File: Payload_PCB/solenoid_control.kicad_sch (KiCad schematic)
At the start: 9 parts, among them Q2 NMOS, Q29 NMOS

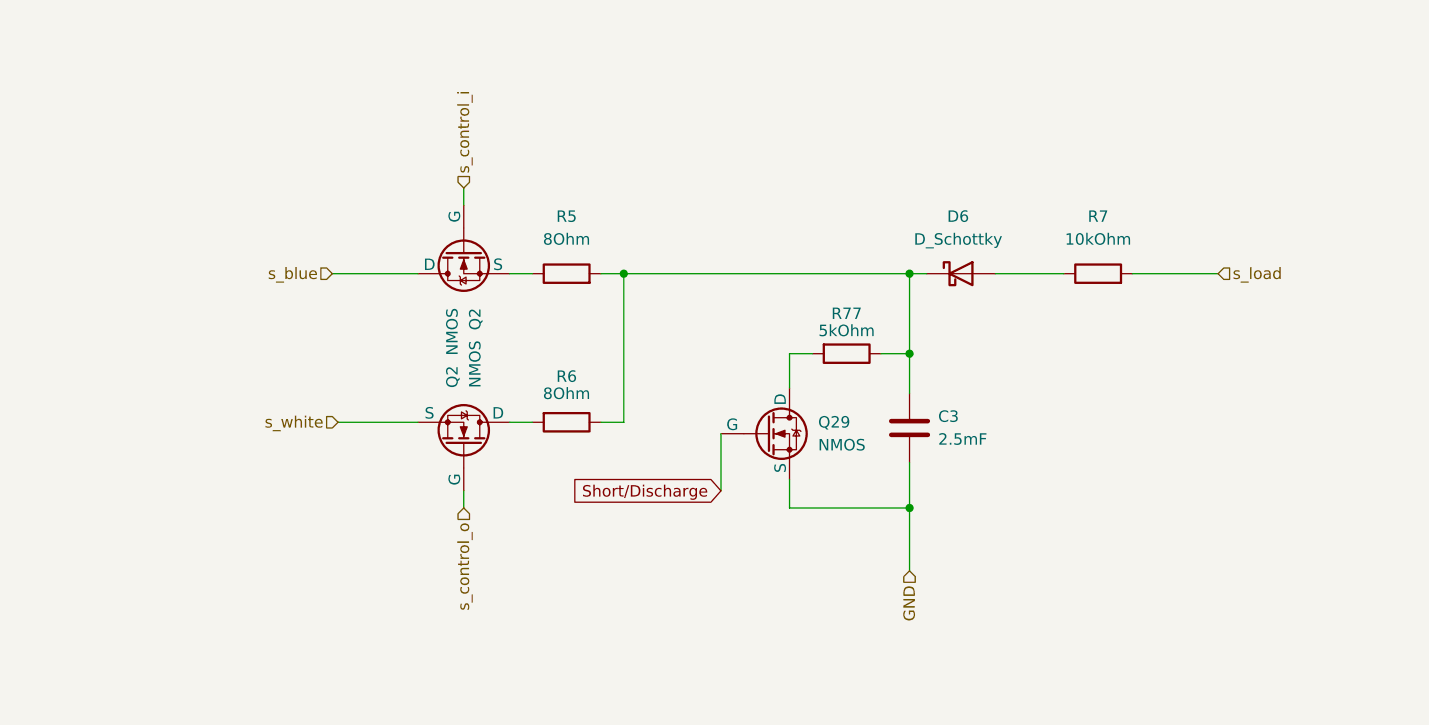
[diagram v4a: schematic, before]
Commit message: Added heating pad, adjustment of page sizes
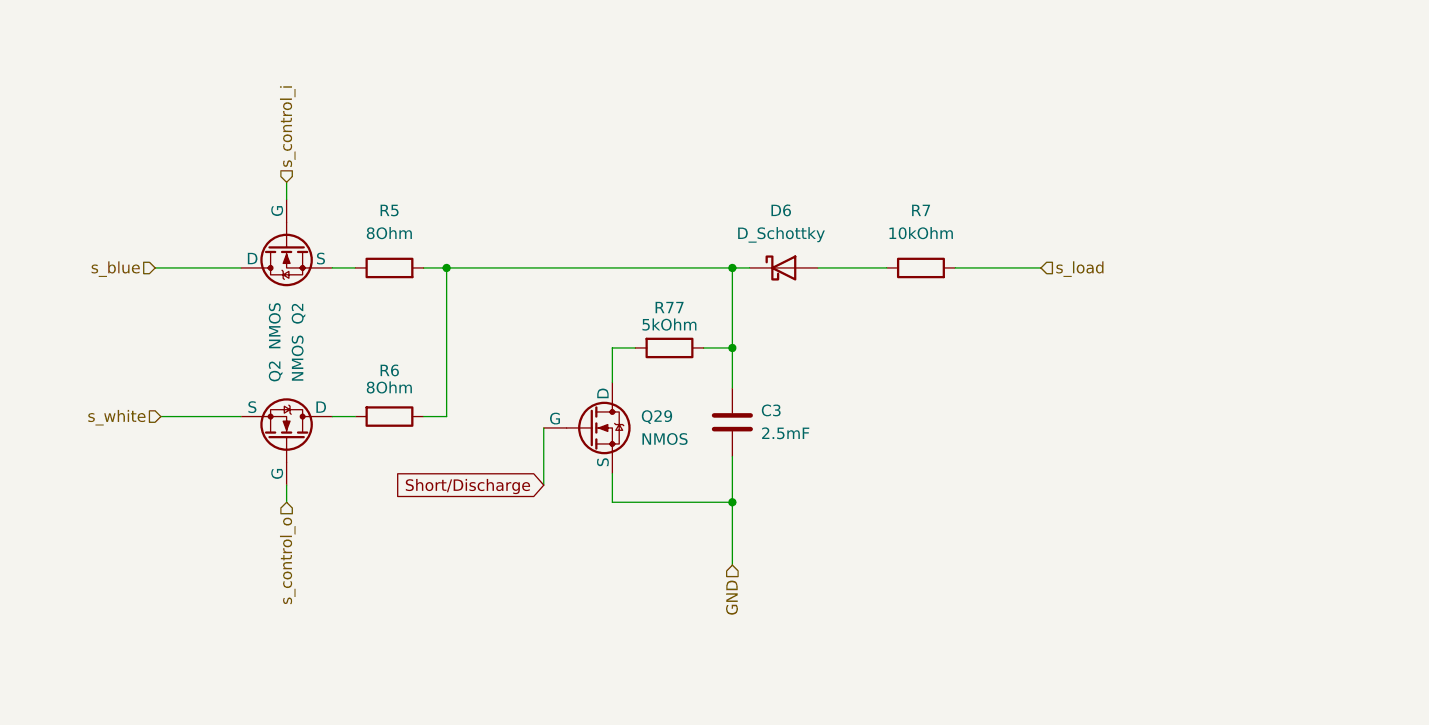
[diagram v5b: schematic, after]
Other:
- moved on the sheet: C3, D6, Q2, Q29, R5, R6, R7, R77

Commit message: Added some actual parts
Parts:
- removed D6: D_Schottky, symbol Device:D_Schottky
- removed Q2 (x2), Q29: NMOS, symbol Simulation_SPICE:NMOS
- added D6: RB511VM-30TE-17, RB511VM30TE17, symbol RB511VM-30TE-17:RB511VM-30TE-17
- added Q28, Q6: SI1308EDL-T1-BE3, SOT65P210X110-3N, symbol SI1308EDL-T1-BE3:SI1308EDL-T1-BE3
- added Q30: SSM3K36TU,LF, SOTFL65P210X75-3N, symbol SSM3K36TU_LF:SSM3K36TU,LF
- R77: value 5kOhm -> 10kOhm
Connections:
- net GND: now also Q30.2 (S)
- net Short/Discharge: now also Q30.1 (G)
- net s_blue: now also Q6.2 (S)
- net s_control_i: now also Q6.1 (G)
- net s_control_o: now also Q28.1 (G)
- net s_white: now also Q28.2 (S)
- net at R77.2: now also Q30.3 (D)
- net at R5.1: now also Q6.3 (D)
- net at C3.2, R5.2, R6.1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: now also D6.1 (K)
- net at R6.2: now also Q28.3 (D)
- net at R7.1: now also D6.2 (A)
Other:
- company: (none) -> SpaceTeam Aachen
- title: (none) -> Solenoid Control
- moved on the sheet: R7

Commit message: some new parts
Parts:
- D6: footprint RB511VM30TE17 -> footprints:RB511VM30TE17
- Q28, Q6: footprint SOT65P210X110-3N -> footprints:SOT65P210X110-3N
- Q30: footprint SOTFL65P210X75-3N -> footprints:SOTFL65P210X75-3N
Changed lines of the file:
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@@
       (effects (font (size 1.27 1.27)))
     )
-    (property "Footprint" "SOT65P210X110-3N" (at -32.69 66.675 0)
+    (property "Footprint" "footprints:SOT65P210X110-3N" (at -32.69 66.675 0)
       (effects (font (size 1.27 1.27)) (justify left top) hide)
     )
@@
       (effects (font (size 1.27 1.27)))
     )
-    (property "Footprint" "SOT65P210X110-3N" (at -32.69 57.785 0)
+    (property "Footprint" "footprints:SOT65P210X110-3N" (at -32.69 57.785 0)
       (effects (font (size 1.27 1.27)) (justify left top) hide)
     )
@@
       (effects (font (size 1.27 1.27)) (justify left))
     )
-    (property "Footprint" "SOTFL65P210X75-3N" (at 107.95 171.755 0)
+    (property "Footprint" "footprints:SOTFL65P210X75-3N" (at 107.95 171.755 0)
       (effects (font (size 1.27 1.27)) (justify left top) hide)
     )
@@
       (effects (font (size 1.27 1.27)))
     )
-    (property "Footprint" "RB511VM30TE17" (at 136.525 151.435 0)
-      (effects (font (size 1.27 1.27)) (justify left top) hide)
-    )
+    (property "Footprint" "footprints:RB511VM30TE17" (at 136.525 151.435 0)
+      (effects (font (size 1.27 1.27)) (justify left top) hide)
+    )

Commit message: Todo notes after review
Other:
- note added: "12 Boost Converter Während Flug laden"
- note added: "Diode zum entladen"
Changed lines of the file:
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@@
     (stroke (width 0) (type default))
+  )
+  (text "Diode zum entladen" (at 40.64 42.545 0)
+    (effects (font (size 1.27 1.27)) (justify left bottom))
+  )
+  (text "12 Boost Converter\nWährend Flug laden" (at 160.655 49.53 0)
+    (effects (font (size 1.27 1.27)) (justify left bottom))
   )
   (label "12V" (at 156.845 53.975 0) (fields_autoplaced)
